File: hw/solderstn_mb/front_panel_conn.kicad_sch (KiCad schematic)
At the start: 21 parts, among them J501 FFC_conn_14p, J502 FFC_conn_14p, J503 JST_S2B-PH-SM4-TB, M501 FFC_retention_clamp, M502 FFC_retention_clamp, Q501 DMG1012T, U501 TLV9051SIDBV

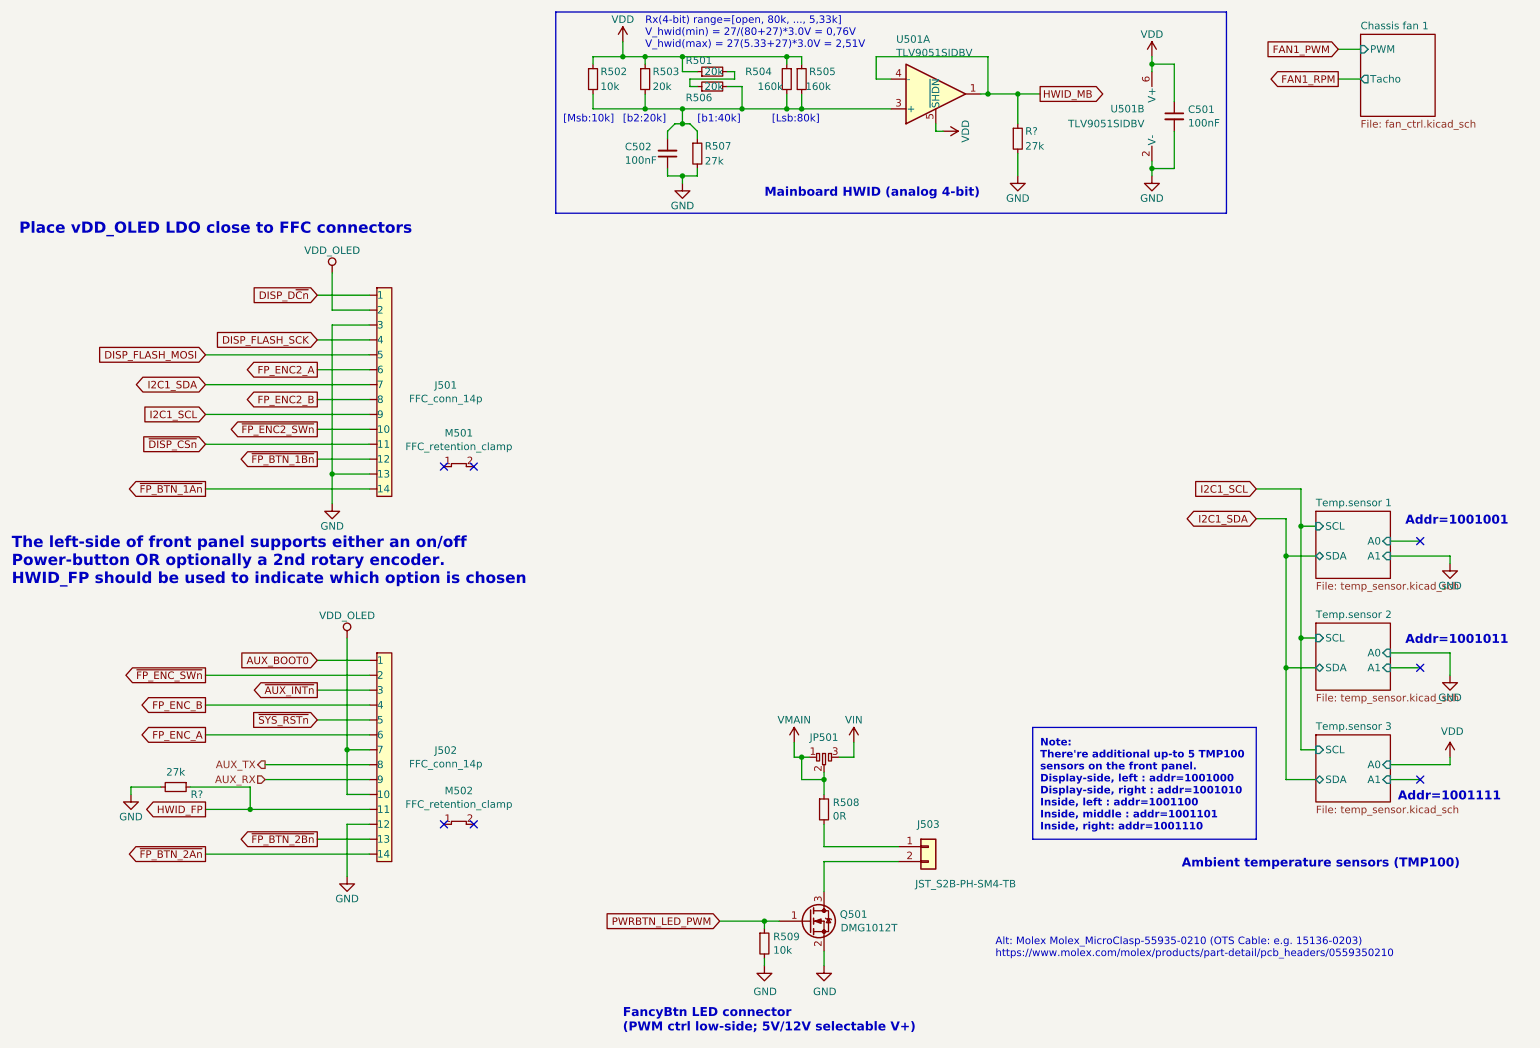
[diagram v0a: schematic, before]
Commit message: Placeholder 3d-models for rear-panel (w. conns), PSU, Bottom-plate, front-panel (w. conns), outer fp
With these placeholder mech. objects, the build-in 3d view of MB pcb features most of the mechanical
objects that constrain components placements. So 3d-view can be used to quickly check and iterate
placements to avoid 3d collisions, without having to first export MB STEP into FreeCAD and muck around
only to have to repeat again for each iteration
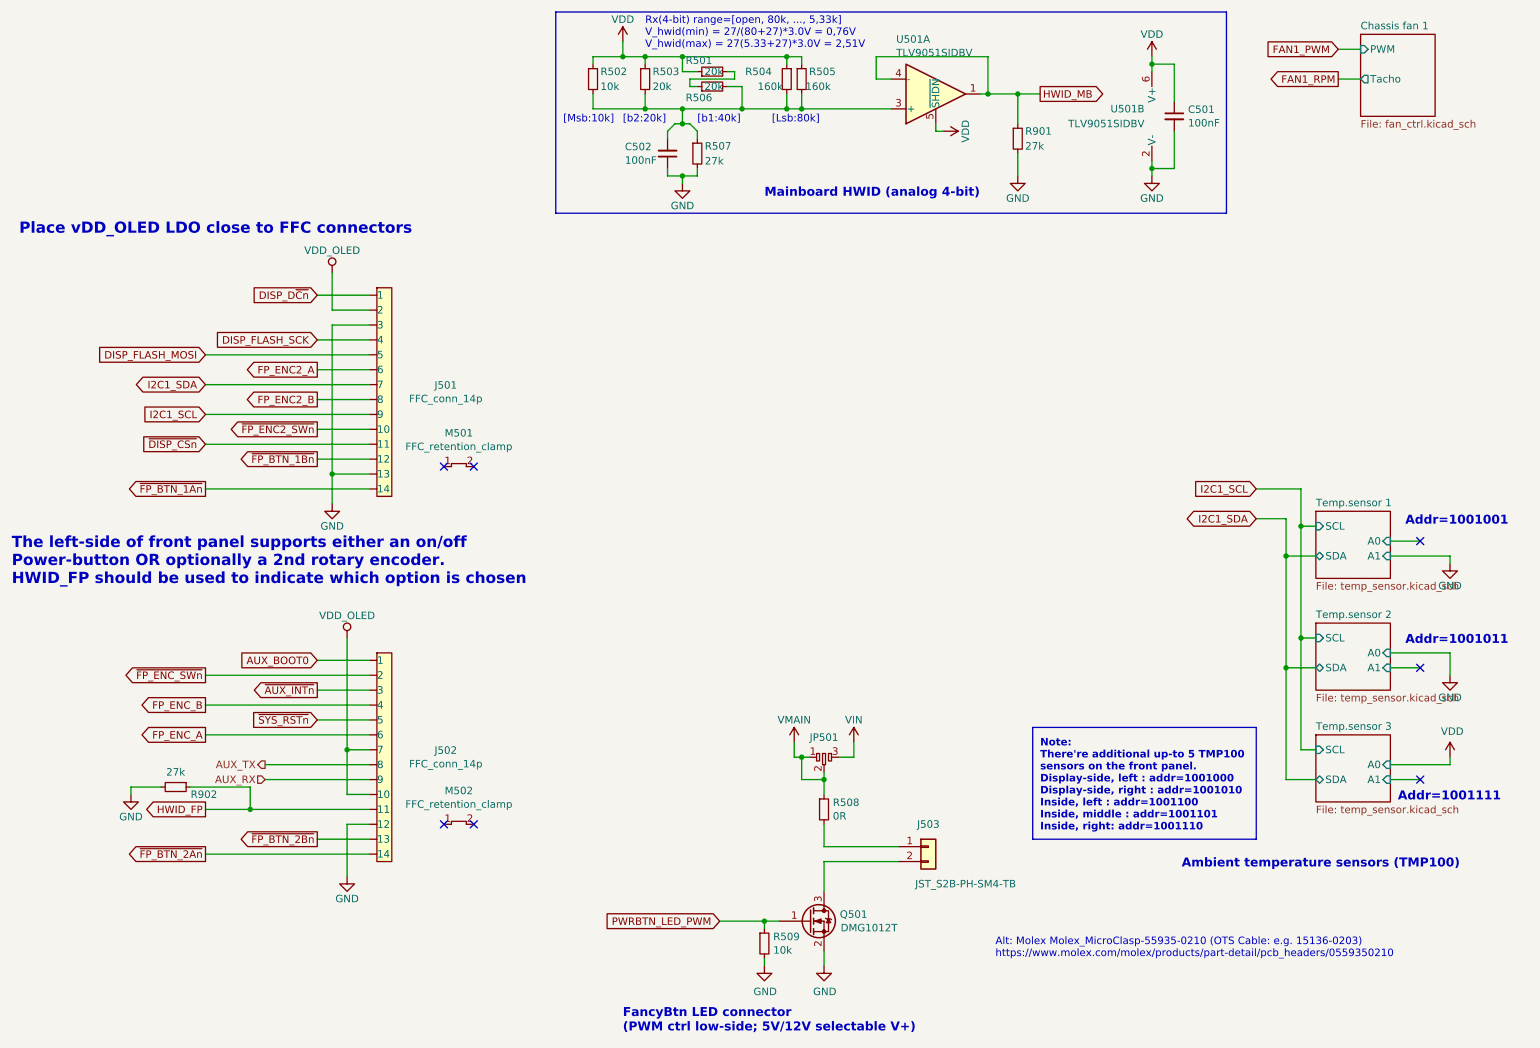
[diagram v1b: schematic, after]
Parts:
- gave numbers to parts that had none: 2
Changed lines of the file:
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@@
   (symbol (lib_id "Device:R_Small") (at 186.69 35.56 0) (unit 1)
     (in_bom yes) (on_board yes)
-    (property "Reference" "R?" (id 0) (at 187.96 34.29 0)
+    (property "Reference" "R901" (id 0) (at 187.96 34.29 0)
       (effects (font (size 1.27 1.27)) (justify left))
     )
@@
   (symbol (lib_id "power:GND") (at 186.69 41.91 0) (unit 1)
     (in_bom yes) (on_board yes)
-    (property "Reference" "#PWR?" (id 0) (at 186.69 48.26 0)
+    (property "Reference" "#PWR0905" (id 0) (at 186.69 48.26 0)
       (effects (font (size 1.27 1.27)) hide)
     )
@@
   (symbol (lib_id "Device:R_Small") (at 43.18 146.05 270) (unit 1)
     (in_bom yes) (on_board yes)
-    (property "Reference" "R?" (id 0) (at 45.72 147.32 90)
+    (property "Reference" "R902" (id 0) (at 45.72 147.32 90)
       (effects (font (size 1.27 1.27)) (justify left))
     )
@@
   (symbol (lib_id "power:GND") (at 35.56 147.32 0) (unit 1)
     (in_bom yes) (on_board yes)
-    (property "Reference" "#PWR?" (id 0) (at 35.56 153.67 0)
+    (property "Reference" "#PWR0906" (id 0) (at 35.56 153.67 0)
       (effects (font (size 1.27 1.27)) hide)
     )
